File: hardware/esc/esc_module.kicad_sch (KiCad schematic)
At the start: 33 parts, among them J4 PHASE_A, J5 PHASE_B, J6 PHASE_C, U1 DRV8300DRGER, U2 STM32G071K8U6, U3 INA180A1

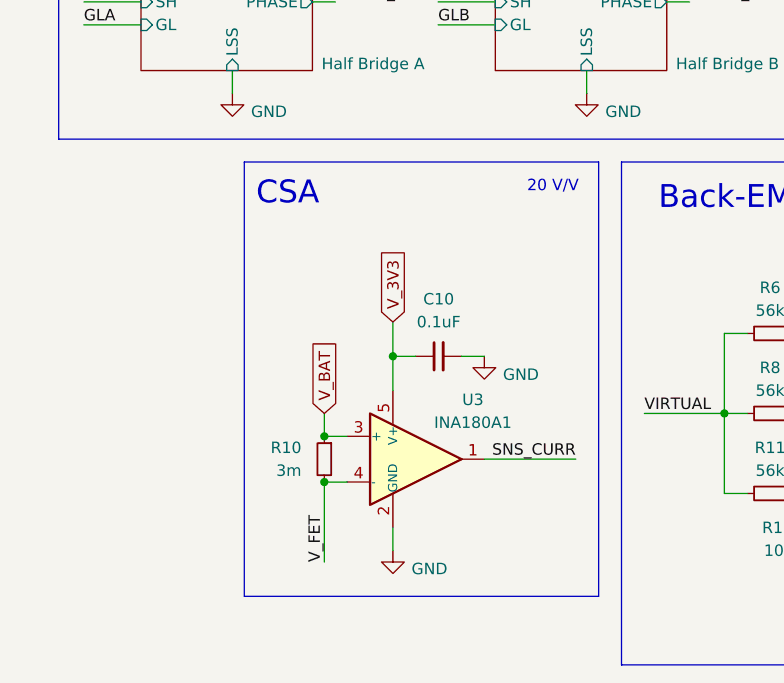
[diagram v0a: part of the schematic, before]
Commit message: h/feat: use hall sensor IC for current sensing instead of CSA; allocate another VBAT layer
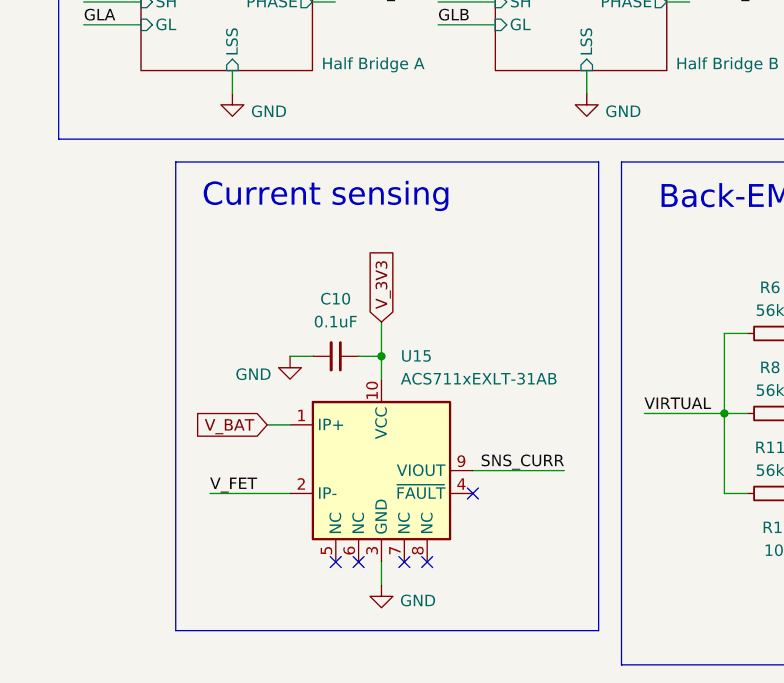
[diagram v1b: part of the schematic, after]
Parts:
- removed R10: 3m, Resistor_SMD:R_2512_6332Metric, symbol Device:R_Small
- removed U3: INA180A1, Stratus:INA180A1IDBVR, symbol Amplifier_Current:INA180A1
- added U15: ACS711xEXLT-31AB, Stratus:ACS711KEXLT-31AB-T, symbol Sensor_Current:ACS711xEXLT-31AB
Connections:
- net GND: now also U15.3 (GND)
- net SNS_CURR: now also U15.9 (VIOUT)
- net V_3V3: now also U15.10 (VCC)
- net V_BAT: now also U15.1 (IP+)
- net V_FET: now also U15.2 (IP-)
- no-connect marks 16 -> 21
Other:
- note added: "Current sensing"
- note removed: "20 V/V"
- note removed: "CSA"
- moved on the sheet: C10

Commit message: chore: add BOM
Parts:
- C10: LCSC# (none) -> C343047; MFR (none) -> TDK; MPN (none) -> CGA2B3X7R1V104KT0Y0F
- C2, C9: LCSC# (none) -> C343047; MFR (none) -> TDK; MPN (none) -> CGA2B3X7R1V104KT0Y0F; Manufacturer_Name Samsung -> (none); Manufacturer_Part_Number CL05A104KA5NNNC -> (none)
- C3: LCSC# (none) -> C22385335; MFR (none) -> Taiyo Yuden; MPN (none) -> TDK105CBJ475MV-F; Manufacturer_Name Samsung -> (none); Manufacturer_Part_Number CL05A104KA5NNNC -> (none)
- C4, C5, C8: LCSC# (none) -> C3835721; MFR (none) -> Murata; MPN (none) -> GRM155R6YA105KE11J; Manufacturer_Name TDK -> (none); Manufacturer_Part_Number C1005X5R1E105K050BC -> (none)
- C59, C60, C64: LCSC# (none) -> C162422; MFR (none) -> Murata; MPN (none) -> GRM21BR6YA106KE43L
- C6: LCSC# (none) -> C343047; MFR (none) -> TDK; MPN (none) -> CGA2B3X7R1V104KT0Y0F; Manufacturer_Name TDK -> (none); Manufacturer_Part_Number C1005X5R1E105K050BC -> (none)
- C7: LCSC# (none) -> C16195875; MFR (none) -> Samsung; MPN (none) -> CL31B106KLHNNNE; Manufacturer_Name Samsung -> (none); Manufacturer_Part_Number CL05A104KA5NNNC -> (none)
- R11, R12, R6, R7, R8, R9: LCSC# (none) -> C114756; MFR (none) -> Yageo; MPN (none) -> RC0402FR-0756KL; Manufacturer_Name Yageo -> (none); Manufacturer_Part_Number RC0402FR-0756KL -> (none)
- R13, R14, R15, R5: LCSC# (none) -> C60490; MFR (none) -> Yageo; MPN (none) -> RC0402FR-0710KL; Manufacturer_Name Yageo -> (none); Manufacturer_Part_Number RC0402FR-0710KL -> (none)
- U1: LCSC# (none) -> C3655801; MFR (none) -> TI; MPN (none) -> DRV8300DRGER
- U15: LCSC# (none) -> C146412; MFR (none) -> Allegro; MPN (none) -> ACS711KEXLT-31AB-T
- U2: LCSC# (none) -> C724237; MFR (none) -> ST; MPN (none) -> STM32G071K8U6

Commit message: h: prep for rev 3; layout, stackup changes
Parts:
- C7: LCSC# C16195875 -> C2175512; MFR Samsung -> Murata; MPN CL31B106KLHNNNE -> GRT31CR6YA106KE01L
- J4, J5, J6, TP1: now left out of the parts list
- R11, R12, R6, R7, R8, R9: value 56k -> 10k; LCSC# C114756 -> C60490; MPN RC0402FR-0756KL -> RC0402FR-0710KL
- R13, R14, R15: value 10k -> 1k; LCSC# C60490 -> C106235; MPN RC0402FR-0710KL -> RC0402FR-071KL
- U2: value STM32G071K8U6 -> STM32G071K(8/B)U6; LCSC# C724237 -> C529350; MPN STM32G071K8U6 -> STM32G071KBU6
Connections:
- no-connect marks 21 -> 17
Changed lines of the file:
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@@
 	)
 	(no_connect
-		(at 74.93 175.26)
-	)
-	(no_connect
 		(at 234.95 83.82)
 	)
@@
 	)
 	(no_connect
-		(at 67.31 175.26)
-	)
-	(no_connect
 		(at 184.15 66.04)
 	)
@@
 	)
 	(no_connect
-		(at 72.39 175.26)
-	)
-	(no_connect
 		(at 234.95 81.28)
 	)
@@
 		(at 49.53 78.74)
 	)
-	(no_connect
-		(at 64.77 175.26)
-	)
 	(wire
 		(pts
@@
 			)
 		)
-		(property "Value" "56k"
+		(property "Value" "10k"
 			(at 143.51 165.1 90)
 			(show_name no)
@@
 			)
 		)
-		(property "Description" "0402 56k"
+		(property "Description" "0402 10k"
 			(at 143.51 167.64 0)
 			(hide yes)
@@
 			)
 		)
-		(property "LCSC#" "C114756"
+		(property "LCSC#" "C60490"
 			(at 143.51 167.64 90)
 			(hide yes)
@@
 			)
 		)
-		(property "MPN" "RC0402FR-0756KL"
+		(property "MPN" "RC0402FR-0710KL"
 			(at 143.51 167.64 90)
 			(hide yes)
@@
 		(body_style 1)
 		(exclude_from_sim no)
-		(in_bom yes)
+		(in_bom no)
 		(on_board yes)
 		(in_pos_files yes)
@@
 			)
 		)
-		(property "Value" "10k"
+		(property "Value" "1k"
 			(at 115.57 173.9899 0)
 			(show_name no)
@@
 			)
 		)
-		(property "Description" "0402 10k"
+		(property "Description" "0402 1k"
 			(at 118.11 172.72 0)
 			(hide yes)
@@
 			)
 		)
-		(property "LCSC#" "C60490"
+		(property "LCSC#" "C106235"
 			(at 118.11 172.72 0)
 			(hide yes)
@@
 			)
 		)
-		(property "MPN" "RC0402FR-0710KL"
+		(property "MPN" "RC0402FR-071KL"
 			(at 118.11 172.72 0)
 			(hide yes)
@@
 			)
 		)
-		(property "Value" "10k"
+		(property "Value" "1k"
 			(at 135.89 173.9899 0)
 			(show_name no)
@@
 			)
 		)
-		(property "Description" "0402 10k"
+		(property "Description" "0402 1k"
 			(at 138.43 172.72 0)
 			(hide yes)
@@
 			)
 		)
-		(property "LCSC#" "C60490"
+		(property "LCSC#" "C106235"
 			(at 138.43 172.72 0)
 			(hide yes)
@@
 			)
 		)
-		(property "MPN" "RC0402FR-0710KL"
+		(property "MPN" "RC0402FR-071KL"
 			(at 138.43 172.72 0)
 			(hide yes)
@@
 			)
 		)
-		(property "Value" "56k"
+		(property "Value" "10k"
 			(at 113.03 156.21 90)
 			(show_name no)
@@
 			)
 		)
-		(property "Description" "0402 56k"
+		(property "Description" "0402 10k"
 			(at 113.03 158.75 0)
 			(hide yes)
@@
 			)
 		)
-		(property "LCSC#" "C114756"
+		(property "LCSC#" "C60490"
 			(at 113.03 158.75 90)
 			(hide yes)
@@
 			)
 		)
-		(property "MPN" "RC0402FR-0756KL"
+		(property "MPN" "RC0402FR-0710KL"
 			(at 113.03 158.75 90)
 			(hide yes)
@@
 			)
 		)
-		(property "Value" "56k"
+		(property "Value" "10k"
 			(at 113.03 147.32 90)
 			(show_name no)
@@
 			)
 		)
-		(property "Description" "0402 56k"
+		(property "Description" "0402 10k"
 			(at 113.03 149.86 0)
 			(hide yes)
@@
 			)
 		)
-		(property "LCSC#" "C114756"
+		(property "LCSC#" "C60490"
 			(at 113.03 149.86 90)
 			(hide yes)
@@
 			)
 		)
-		(property "MPN" "RC0402FR-0756KL"
+		(property "MPN" "RC0402FR-0710KL"
 			(at 113.03 149.86 90)
 			(hide yes)
@@
 			)
 		)
-		(property "Value" "STM32G071K8U6"
+		(property "Value" "STM32G071K(8/B)U6"
 			(at 220.218 41.402 0)
 			(show_name no)
@@
 			)
 		)
-		(property "Datasheet" "https://www.st.com/resource/en/datasheet/stm32g071c8.pdf"
+		(property "Datasheet" "https://www.st.com/resource/en/datasheet/stm32g071k8.pdf"
 			(at 184.15 48.26 0)
 			(hide yes)
@@
 			)
 		)
-		(property "LCSC#" "C724237"
+		(property "LCSC#" "C529350"
 			(at 184.15 48.26 0)
 			(hide yes)
@@
 			)
 		)
-		(property "MPN" "STM32G071K8U6"
+		(property "MPN" "STM32G071KBU6"
 			(at 184.15 48.26 0)
 			(hide yes)
@@
 			)
 		)
-		(property "Value" "56k"
+		(property "Value" "10k"
 			(at 143.51 156.21 90)
 			(show_name no)
@@
 			)
 		)
-		(property "Description" "0402 56k"
+		(property "Description" "0402 10k"
 			(at 143.51 158.75 0)
 			(hide yes)
@@
 			)
 		)
-		(property "LCSC#" "C114756"
+		(property "LCSC#" "C60490"
 			(at 143.51 158.75 90)
 			(hide yes)
@@
 			)
 		)
-		(property "MPN" "RC0402FR-0756KL"
+		(property "MPN" "RC0402FR-0710KL"
 			(at 143.51 158.75 90)
 			(hide yes)
@@
 		(body_style 1)
 		(exclude_from_sim no)
-		(in_bom yes)
+		(in_bom no)
 		(on_board yes)
 		(in_pos_files yes)
@@
 			)
 		)
-		(property "Value" "56k"
+		(property "Value" "10k"
 			(at 113.03 165.1 90)
 			(show_name no)
@@
 			)
 		)
-		(property "Description" "0402 56k"
+		(property "Description" "0402 10k"
 			(at 113.03 167.64 0)
 			(hide yes)
@@
 			)
 		)
-		(property "LCSC#" "C114756"
+		(property "LCSC#" "C60490"
 			(at 113.03 167.64 90)
 			(hide yes)
@@
 			)
 		)
-		(property "MPN" "RC0402FR-0756KL"
+		(property "MPN" "RC0402FR-0710KL"
 			(at 113.03 167.64 90)
 			(hide yes)
@@
 			)
 		)
-		(property "Value" "10k"
+		(property "Value" "1k"
 			(at 125.73 173.9899 0)
 			(show_name no)
@@
 			)
 		)
-		(property "Description" "0402 10k"
+		(property "Description" "0402 1k"
 			(at 128.27 172.72 0)
 			(hide yes)
@@
 			)
 		)
-		(property "LCSC#" "C60490"
+		(property "LCSC#" "C106235"
 			(at 128.27 172.72 0)
 			(hide yes)
@@
 			)
 		)
-		(property "MPN" "RC0402FR-0710KL"
+		(property "MPN" "RC0402FR-071KL"
 			(at 128.27 172.72 0)
 			(hide yes)
@@
 		(body_style 1)
 		(exclude_from_sim no)
-		(in_bom yes)
+		(in_bom no)
 		(on_board yes)
 		(in_pos_files yes)
@@
 			)
 		)
-		(property "LCSC#" "C16195875"
+		(property "LCSC#" "C2175512"
 			(at 140.97 57.15 0)
 			(hide yes)
@@
 			)
 		)
-		(property "MFR" "Samsung"
+		(property "MFR" "Murata"
 			(at 140.97 57.15 0)
 			(hide yes)
@@
 			)
 		)
-		(property "MPN" "CL31B106KLHNNNE"
+		(property "MPN" "GRT31CR6YA106KE01L"
 			(at 140.97 57.15 0)
 			(hide yes)
@@
 		(body_style 1)
 		(exclude_from_sim no)
-		(in_bom yes)
+		(in_bom no)
 		(on_board yes)
 		(in_pos_files yes)
@@
 		(pin "4"
 		)
-		(pin "6"
-		)
-		(pin "7"
-		)
 		(pin "1"
 		)
 		(pin "3"
 		)
-		(pin "8"
-		)
-		(pin "5"
-		)
 		(instances
 			(project "esc"
@@
 			)
 		)
-		(property "Value" "56k"
+		(property "Value" "10k"
 			(at 143.51 147.32 90)
 			(show_name no)
@@
 			)
 		)
-		(property "Description" "0402 56k"
+		(property "Description" "0402 10k"
 			(at 143.51 149.86 0)
 			(hide yes)
@@
 			)
 		)
-		(property "LCSC#" "C114756"
+		(property "LCSC#" "C60490"
 			(at 143.51 149.86 90)
 			(hide yes)
@@
 			)
 		)
-		(property "MPN" "RC0402FR-0756KL"
+		(property "MPN" "RC0402FR-0710KL"
 			(at 143.51 149.86 90)
 			(hide yes)
